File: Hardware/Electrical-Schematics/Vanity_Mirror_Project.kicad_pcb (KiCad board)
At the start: 2 copper layers, 40 parts, among them J1 USB_C_Receptacle_USB2.0_14P, SW1 RST, U1 CH340C, U2 ESP-12F, U3 USBLC6-2SC6, U4 XL1509-3.3, U5 SN74AHCT125N, U6 MPR121QR2

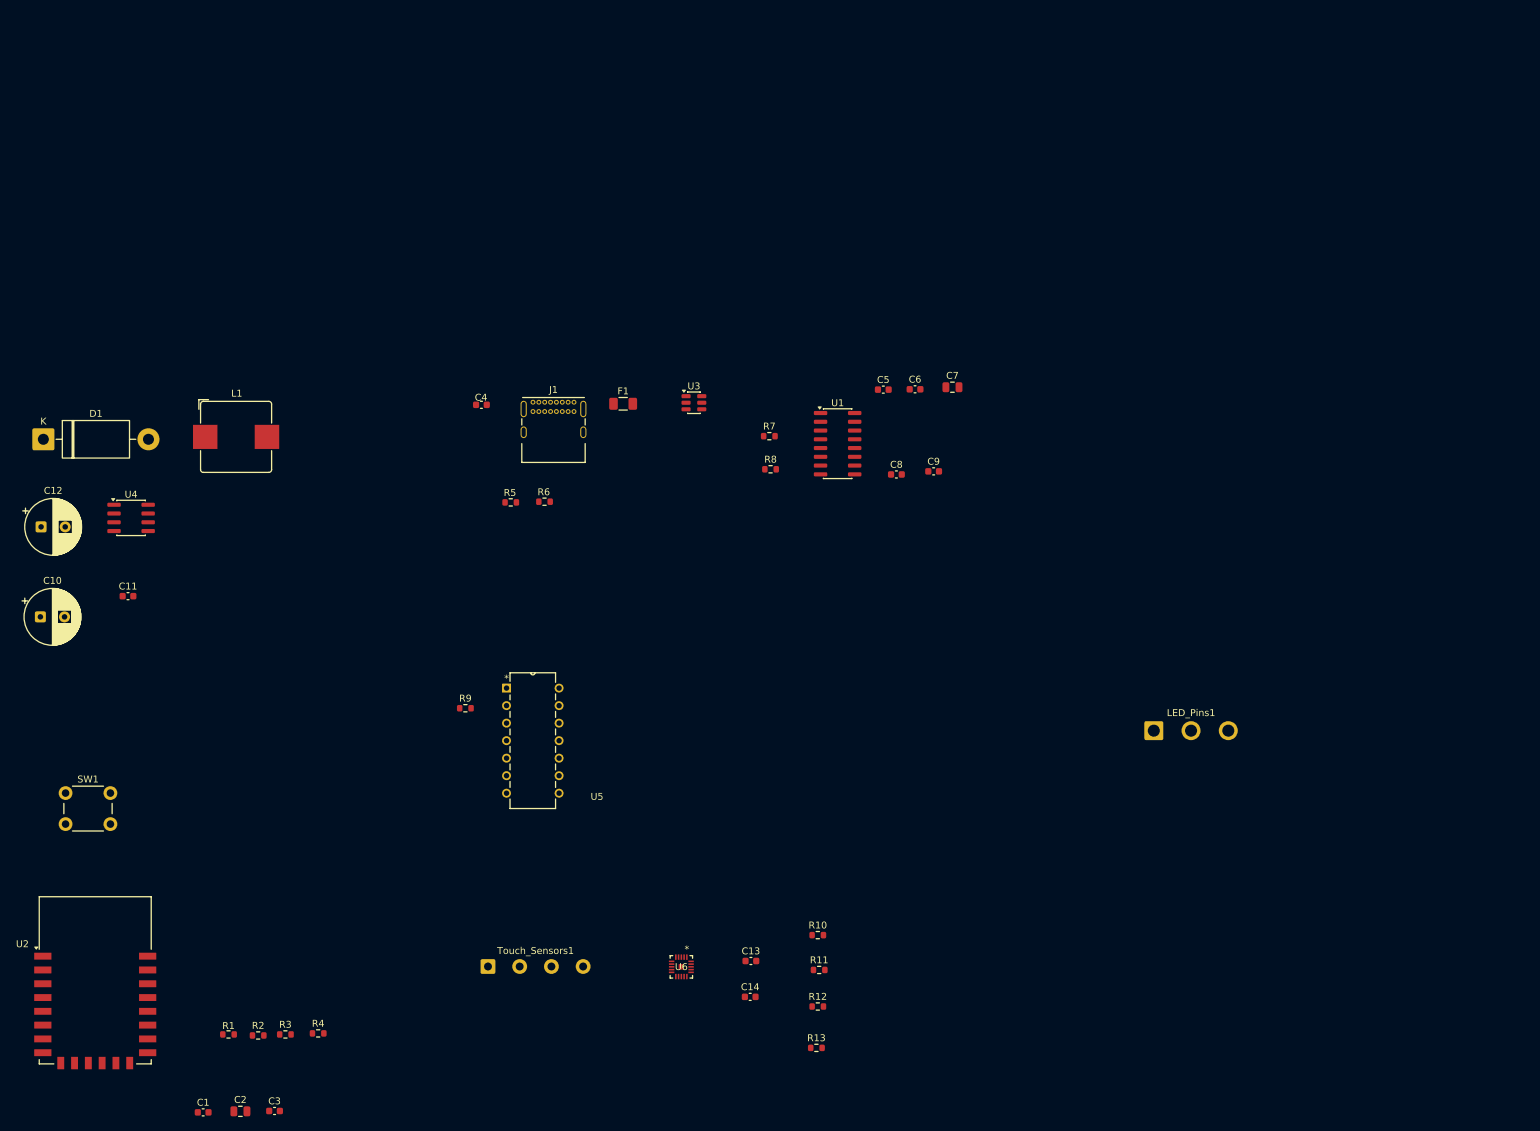
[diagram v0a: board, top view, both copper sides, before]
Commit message: PCB Design Progress
Made progress with the PCB design and reorganized the gitignores so that it works.
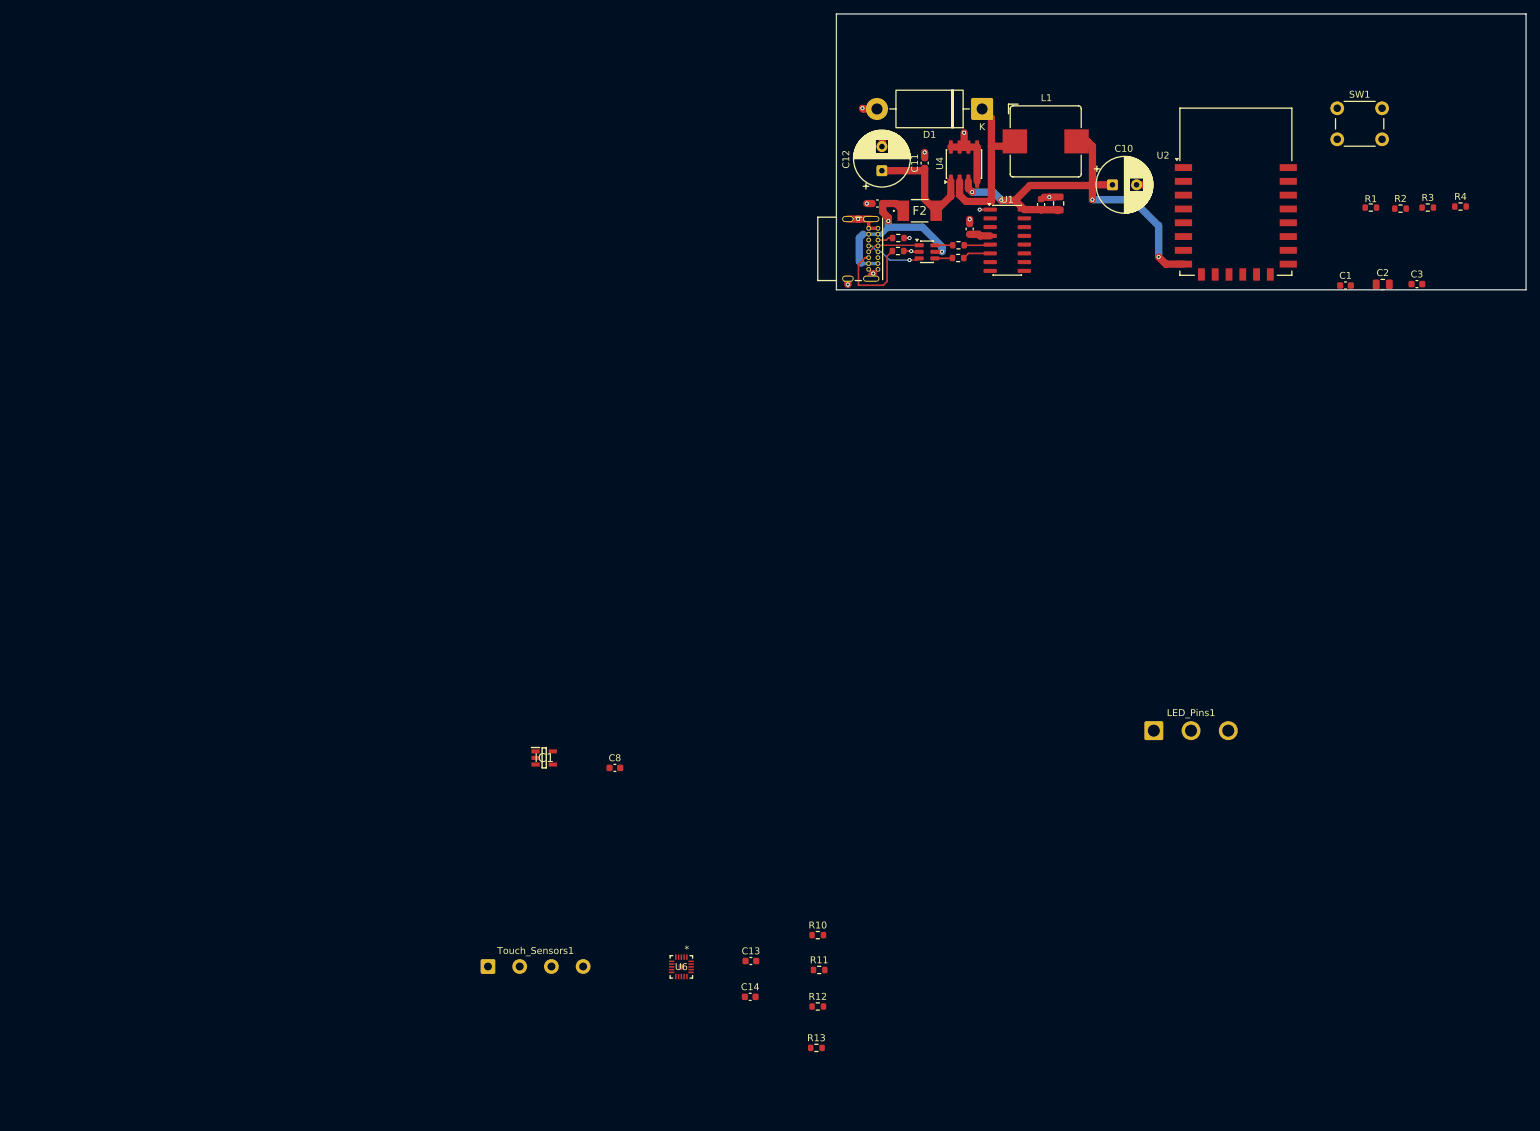
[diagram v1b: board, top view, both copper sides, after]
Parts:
- removed C9: 0.1uF, Capacitor_SMD:C_0603_1608Metric
- removed F1: Polyfuse, Fuse:Fuse_1206_3216Metric
- removed R9: 330, Resistor_SMD:R_0603_1608Metric
- removed U5: SN74AHCT125N, VanityMirror_FootPrints:SN74AHCT125N
- added F2: MF-MSMF300_6X-2, VanityMirror_FootPrints:MFMSMF3006X2, F.Cu at (163.8, 48.6)
- added IC1: SN74LV1T34QDBVRQ1, VanityMirror_FootPrints:SOT95P280X145-5N, F.Cu at (109.3, 128.0)
- moved SW1 209.4 mm to (224.3, 33.8)
- moved C1 204.5 mm to (225.5, 59.5)
- moved C2 204.5 mm to (230.9, 59.3)
- moved R1 204.5 mm to (229.2, 48.1)
- moved R3 204.5 mm to (237.4, 48.1)
- moved R4 204.5 mm to (242.2, 48.0)
- moved C3 204.5 mm to (235.8, 59.2)
- moved R2 204.5 mm to (233.5, 48.3)
- moved U2 201.1 mm to (209.6, 45.9)
- moved C10 167.6 mm to (191.7, 44.9)
- moved D1 144.3 mm to (172.8, 33.9), turned to 180 degrees
- moved C12 132.4 mm to (158.3, 42.8), turned to 90 degrees
- moved C11 131.5 mm to (164.5, 41.7), turned to 90 degrees
- moved U4 131.2 mm to (170.2, 41.8), turned to 90 degrees
- moved L1 125.0 mm to (182.0, 38.5)
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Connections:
- C4 pad 1: +5V -> Net-(U3-VBUS)
- C8 pad 1: Net-(U1-~{DTR}) -> +5V
- C8 pad 2: /~{DTR} -> GND
- J1 pad A4: +5V -> Net-(U3-VBUS)
- J1 pad A9: +5V -> Net-(U3-VBUS)
- J1 pad B4: +5V -> Net-(U3-VBUS)
- J1 pad B9: +5V -> Net-(U3-VBUS)
- U1 pad 13: Net-(U1-~{DTR}) -> /~{DTR}
- U1 pad 14: Net-(U1-~{RTS}) -> /~{RTS}
- U3 pad 5: +5V -> Net-(U3-VBUS)
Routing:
- net +3.3V: track 0.00 -> 60.9 mm, vias 0 -> 4
- net GND: track 0.00 -> 35.6 mm, vias 0 -> 14
- net Net-(U3-VBUS): track 0.00 -> 29.0 mm, vias 0 -> 2
- net Net-(D1-K): track 0.00 -> 24.7 mm
- net +5V: track 0.00 -> 18.3 mm
- net Net-(J1-CC2): track 0.00 -> 14.1 mm
- net Net-(J1-D--PadA7): track 0.00 -> 8.67 mm, vias 0 -> 1
- net Net-(J1-D+-PadA6): track 0.00 -> 7.93 mm
- net Net-(U1-UD-): track 0.00 -> 4.10 mm
- net Net-(U1-UD+): track 0.00 -> 3.81 mm
- net Net-(U1-V3): track 0.00 -> 3.07 mm
- net Net-(R7-Pad2): track 0.00 -> 2.60 mm
- net Net-(R8-Pad2): track 0.00 -> 2.57 mm
- net Net-(J1-CC1): track 0.00 -> 2.25 mm
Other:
- board outline added: 100 x 40 mm

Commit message: Initial PCB layout and Schematic Revisions
Revised some wiring in the schematic and fixed some wiring mistakes. Created an initial layout for the PCB
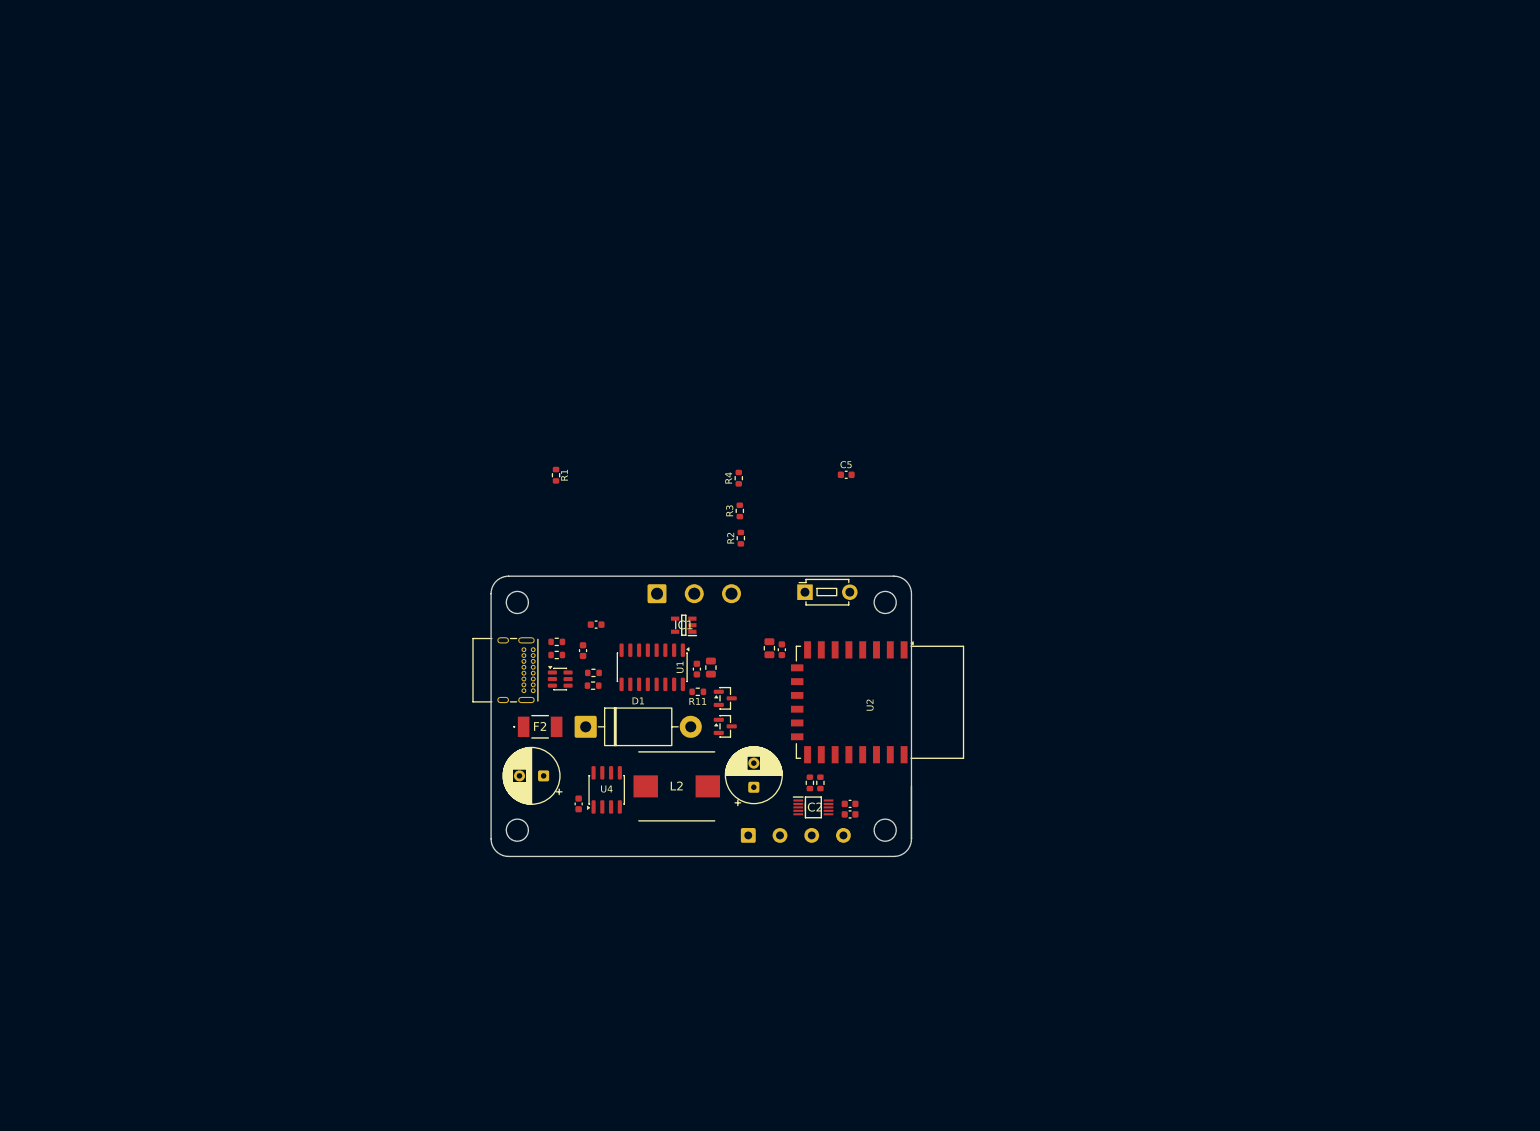
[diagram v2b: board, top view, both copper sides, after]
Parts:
- removed C14, C3: 0.1uF, Capacitor_SMD:C_0603_1608Metric
- removed L1: 22uH, Inductor_SMD:L_Bourns_SRP1038C_10.0x10.0mm
- removed R12, R13: 10k, Resistor_SMD:R_0603_1608Metric
- removed U6: MPR121QR2, VanityMirror_FootPrints:QFN20_FRE
- added C9: 0.1uF, Capacitor_SMD:C_0603_1608Metric, F.Cu at (153.7, 136.1)
- added H1: MountingHole, MountingHole:MountingHole_3.2mm_M3, F.Cu at (158.8, 138.4)
- added H2: MountingHole, MountingHole:MountingHole_3.2mm_M3, F.Cu at (158.8, 105.4)
- added H3: MountingHole, MountingHole:MountingHole_3.2mm_M3, F.Cu at (105.4, 105.4)
- added H4: MountingHole, MountingHole:MountingHole_3.2mm_M3, F.Cu at (105.4, 138.4)
- added IC2: FDC1004QDGSRQ1, VanityMirror_FootPrints:SOP50P490X110-10N, F.Cu at (148.3, 135.1)
- added L2: 22uH, VanityMirror_FootPrints:INDPM110100X400N, F.Cu at (128.5, 132.1)
- added Q1: 2N7002, Package_TO_SOT_SMD:SOT-23, F.Cu at (135.6, 123.4)
- added Q2: 2N7002, Package_TO_SOT_SMD:SOT-23, F.Cu at (135.6, 119.3)
- added R9: 4.7k, Resistor_SMD:R_0603_1608Metric, F.Cu at (149.4, 131.6)
- C13: value 0.1uF -> 1uF
- R10: value 75k -> 4.7k
- R11: value 10k -> 220
- SW1: footprint Button_Switch_THT:SW_PUSH_6mm -> Button_Switch_THT:SW_PUSH_1P1T_6x3.5mm_H4.3_APEM_MJTP1243
- moved R1 124.4 mm to (111.0, 87.0), turned to -90 degrees
- moved R4 111.8 mm to (137.5, 87.4), turned to 90 degrees
- moved R3 109.0 mm to (137.7, 92.1), turned to 90 degrees
- moved R2 106.9 mm to (137.8, 96.1), turned to 90 degrees
- moved D1 106.4 mm to (115.3, 123.4), turned to 0 degrees
- moved C11 105.6 mm to (114.3, 134.6)
- moved U4 104.5 mm to (118.4, 132.6)
- moved SW1 104.3 mm to (147.1, 103.9)
- moved C2 103.4 mm to (142.0, 112.0), turned to 90 degrees
- moved C10 101.7 mm to (139.7, 132.2), turned to 90 degrees
- moved C12 100.5 mm to (109.2, 130.6), turned to 180 degrees
- moved C1 97.3 mm to (143.8, 112.3), turned to 90 degrees
- moved F2 92.9 mm to (108.7, 123.4)
- moved U2 90.3 mm to (158.0, 119.9), turned to -90 degrees
- moved C7 84.1 mm to (133.5, 114.9)
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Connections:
- C5 pad 1: Net-(U1-V3) -> GND
- C5 pad 2: GND -> Net-(Q2-D)
- R1 pad 1: Net-(U2-~{RST}) -> Net-(U2-EN)
- R10 pad 1: GND -> /SCL
- R10 pad 2: Net-(U6-REXT) -> +3.3V
- R11 pad 1: /SCL -> Net-(Q2-G)
- R11 pad 2: +3.3V -> /~{RTS}
- R2 pad 1: /~{DTR} -> Net-(Q2-D)
- R3 pad 1: /~{RTS} -> Net-(Q1-D)
- SW1 pad 2: Net-(U2-~{RST}) -> Net-(Q2-D)
- U1 pad 4: Net-(U1-V3) -> +3.3V
- U2 pad 1: Net-(U2-~{RST}) -> Net-(Q2-D)
- U2 pad 18: /~{RTS} -> Net-(Q1-D)
- U2 pad 3: /~{DTR} -> Net-(U2-EN)
- U2 pad 7: /~{IRQ} -> unconnected-(U2-GPIO13-Pad7)
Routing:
- net +3.3V: track 60.9 -> 0.00 mm, vias 4 -> 0
- net GND: track 35.6 -> 0.00 mm, vias 14 -> 0
- net Net-(U3-VBUS): track 29.0 -> 0.00 mm, vias 2 -> 0
- net Net-(D1-K): track 24.7 -> 0.00 mm
- net +5V: track 18.3 -> 0.00 mm
- net Net-(J1-CC2): track 14.1 -> 0.00 mm
- net Net-(J1-D--PadA7): track 8.67 -> 0.00 mm, vias 1 -> 0
- net Net-(J1-D+-PadA6): track 7.93 -> 0.00 mm
- net Net-(U1-UD-): track 4.10 -> 0.00 mm
- net Net-(U1-UD+): track 3.81 -> 0.00 mm
- net Net-(U1-V3): track 3.07 -> 0.00 mm
- net Net-(R7-Pad2): track 2.60 -> 0.00 mm
- net Net-(R8-Pad2): track 2.57 -> 0.00 mm
- net Net-(J1-CC1): track 2.25 -> 0.00 mm
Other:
- board size 100 x 40 mm -> 61 x 40.6 mm
